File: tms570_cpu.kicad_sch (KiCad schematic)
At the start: 50 parts, among them J3 FTSH-105-01-L-DV-K, U2 TMS570LS0914APGEQQ1

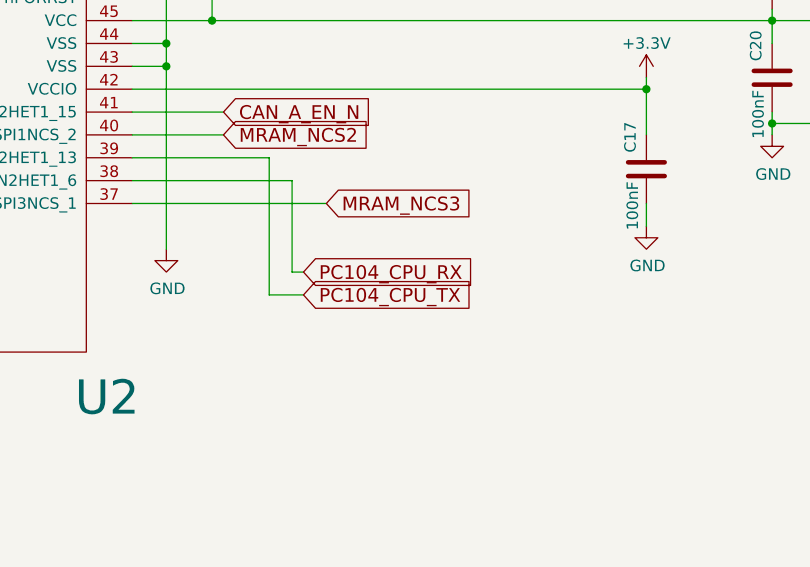
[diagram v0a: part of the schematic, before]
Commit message: Remove the serial connections from the PC104
The USB connection has proven itself, so it shouldn't be needed on later
boards.  This allowed some routing simplification.

Signed-off-by: Corey Minyard <corey@minyard.net>
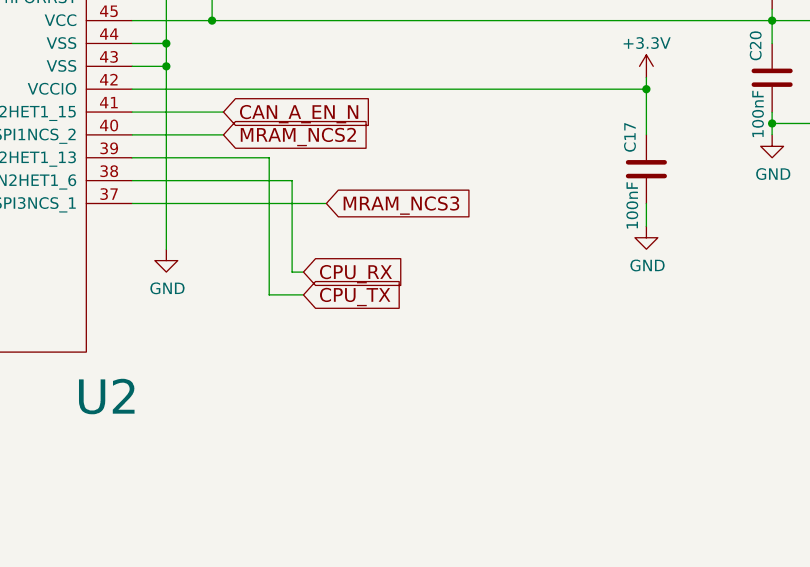
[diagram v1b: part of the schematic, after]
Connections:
- net PC104_CPU_RX renamed CPU_RX
- net PC104_CPU_TX renamed CPU_TX
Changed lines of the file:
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@@
 		)
 	)
-	(global_label "PC104_CPU_TX"
+	(global_label "CPU_TX"
 		(shape input)
 		(at 300.99 193.04 0)
@@
 		)
 	)
-	(global_label "PC104_CPU_RX"
+	(global_label "CPU_RX"
 		(shape input)
 		(at 300.99 190.5 0)

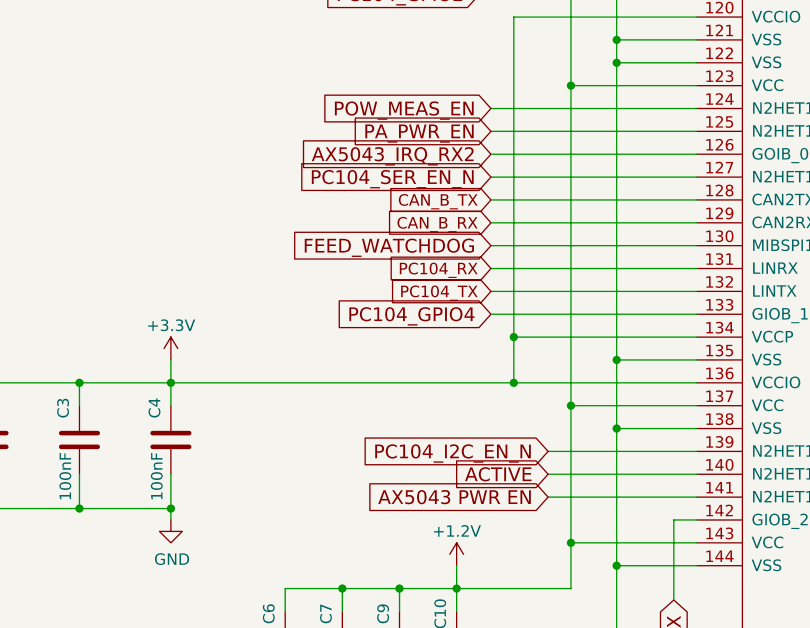
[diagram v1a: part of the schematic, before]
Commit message: Replace the switches for the PC104 I2C and UART with a TMUX2821
It's smaller and has better characteristics.  Particularly, it doesn't
require a pull-up, it's pulled down internally.  Pull down avoids CMOS
latch up on the control pin out of the TMS570.

Signed-off-by: Corey Minyard <corey@minyard.net>
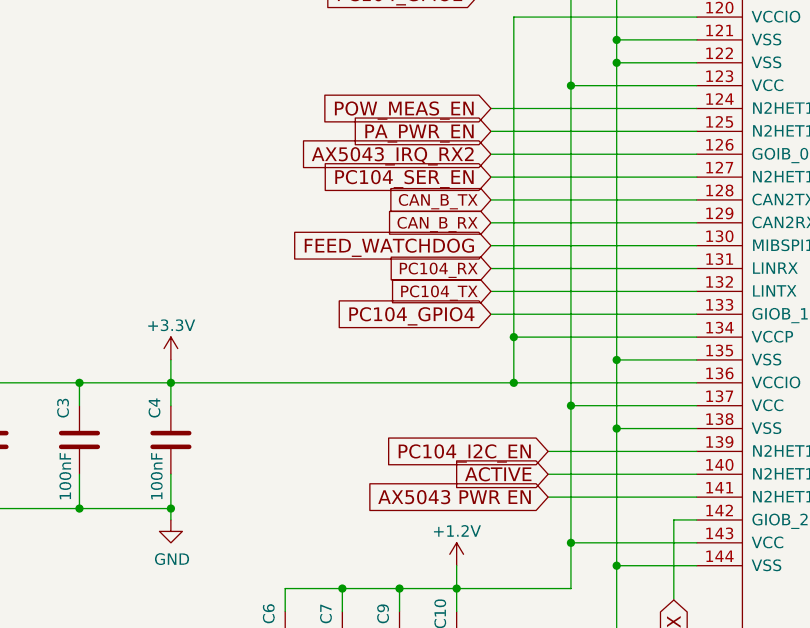
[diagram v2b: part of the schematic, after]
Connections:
- net PC104_I2C_EN_N renamed PC104_I2C_EN
- net PC104_SER_EN_N renamed PC104_SER_EN
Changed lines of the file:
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@@
 		)
 	)
-	(global_label "PC104_SER_EN_N"
+	(global_label "PC104_SER_EN"
 		(shape input)
 		(at 127 142.24 180)
@@
 		)
 	)
-	(global_label "PC104_I2C_EN_N"
+	(global_label "PC104_I2C_EN"
 		(shape input)
 		(at 133.35 172.72 180)

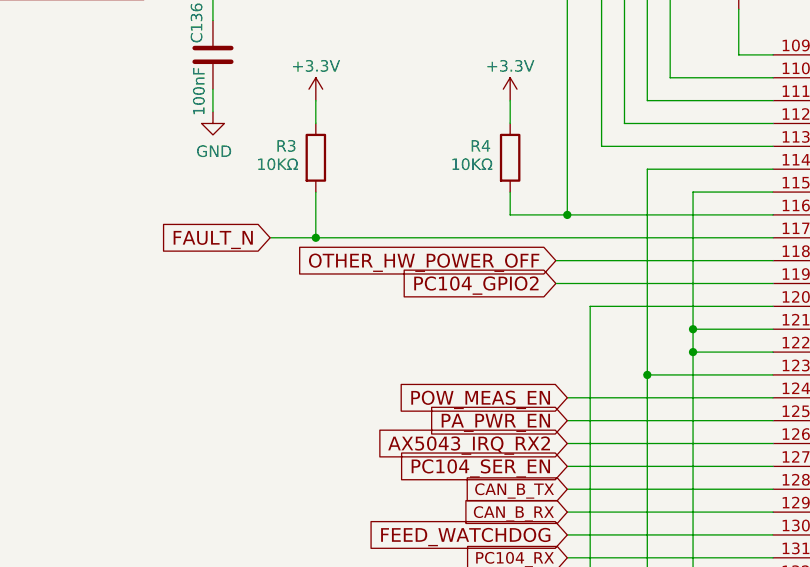
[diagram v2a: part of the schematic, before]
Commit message: Tie the bootstrap load (BSL) lines into the USB chip
Through MOSFETs avoid CMOS latch up.  This will let GPIO lines on the
USB chip start the BSL process.

Signed-off-by: Corey Minyard <corey@minyard.net>
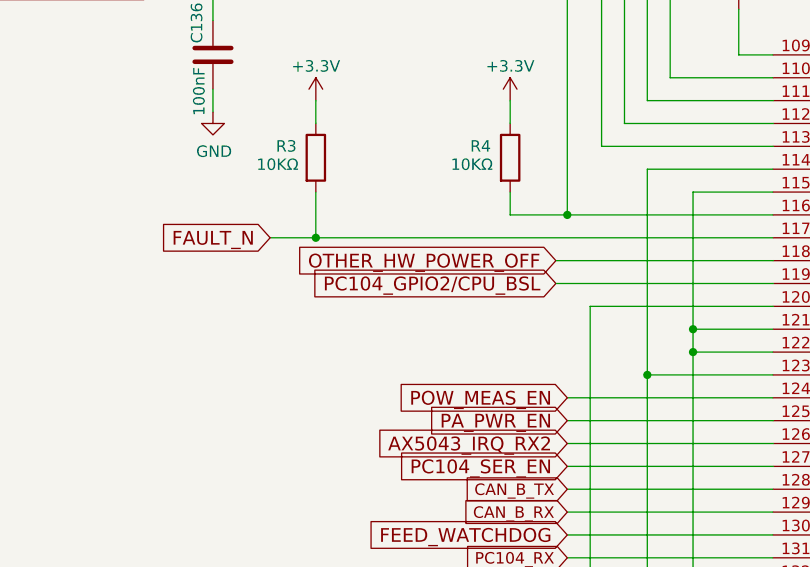
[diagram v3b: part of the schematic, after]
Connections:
- net PC104_GPIO2 renamed PC104_GPIO2/CPU_BSL
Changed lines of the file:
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@@
 		)
 	)
-	(global_label "PC104_GPIO2"
+	(global_label "PC104_GPIO2{slash}CPU_BSL"
 		(shape input)
 		(at 125.73 121.92 180)

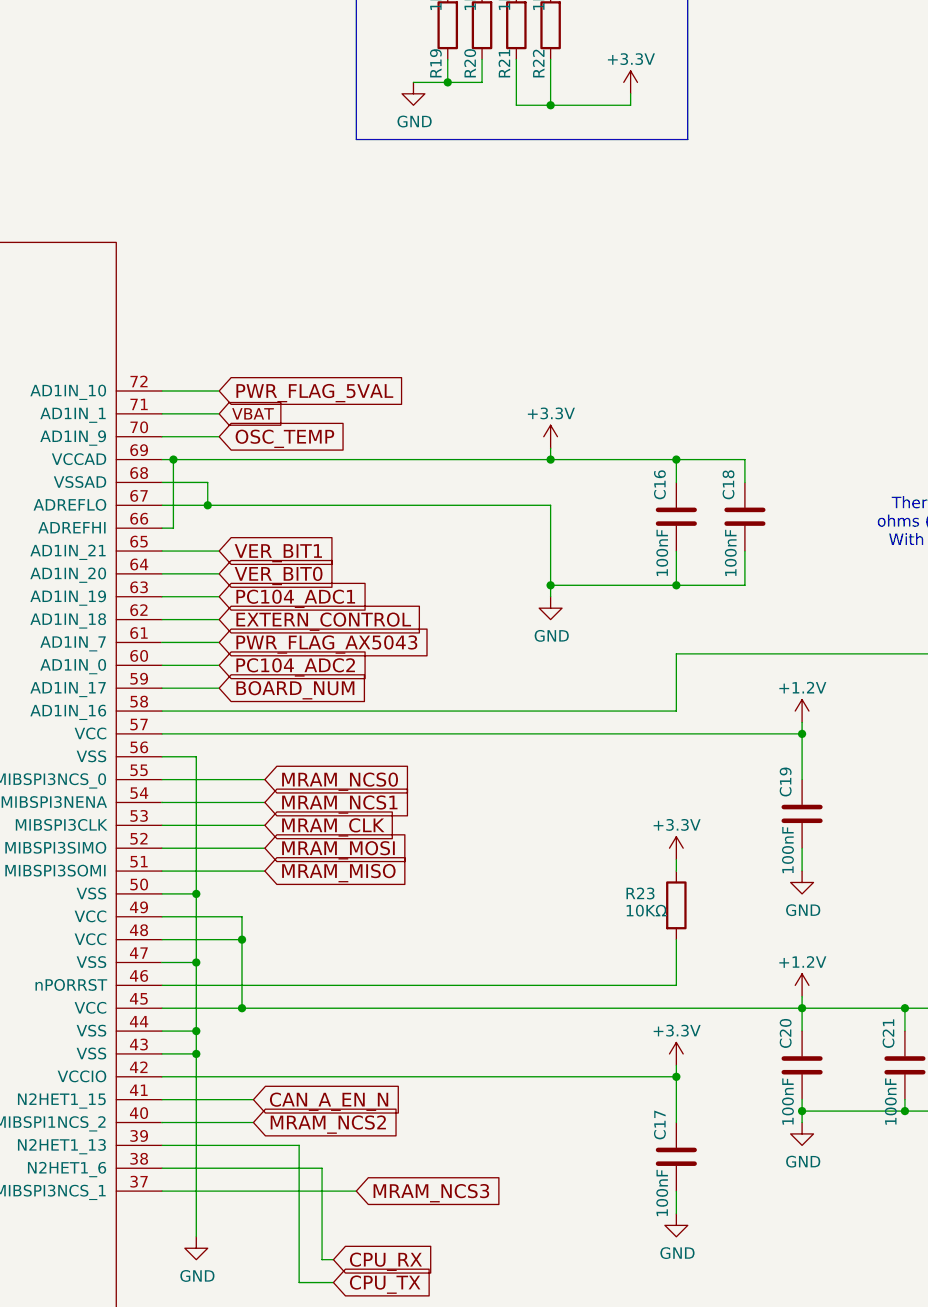
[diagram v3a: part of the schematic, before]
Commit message: Fix various issues from kicad updates
Signed-off-by: Corey Minyard <corey@minyard.net>
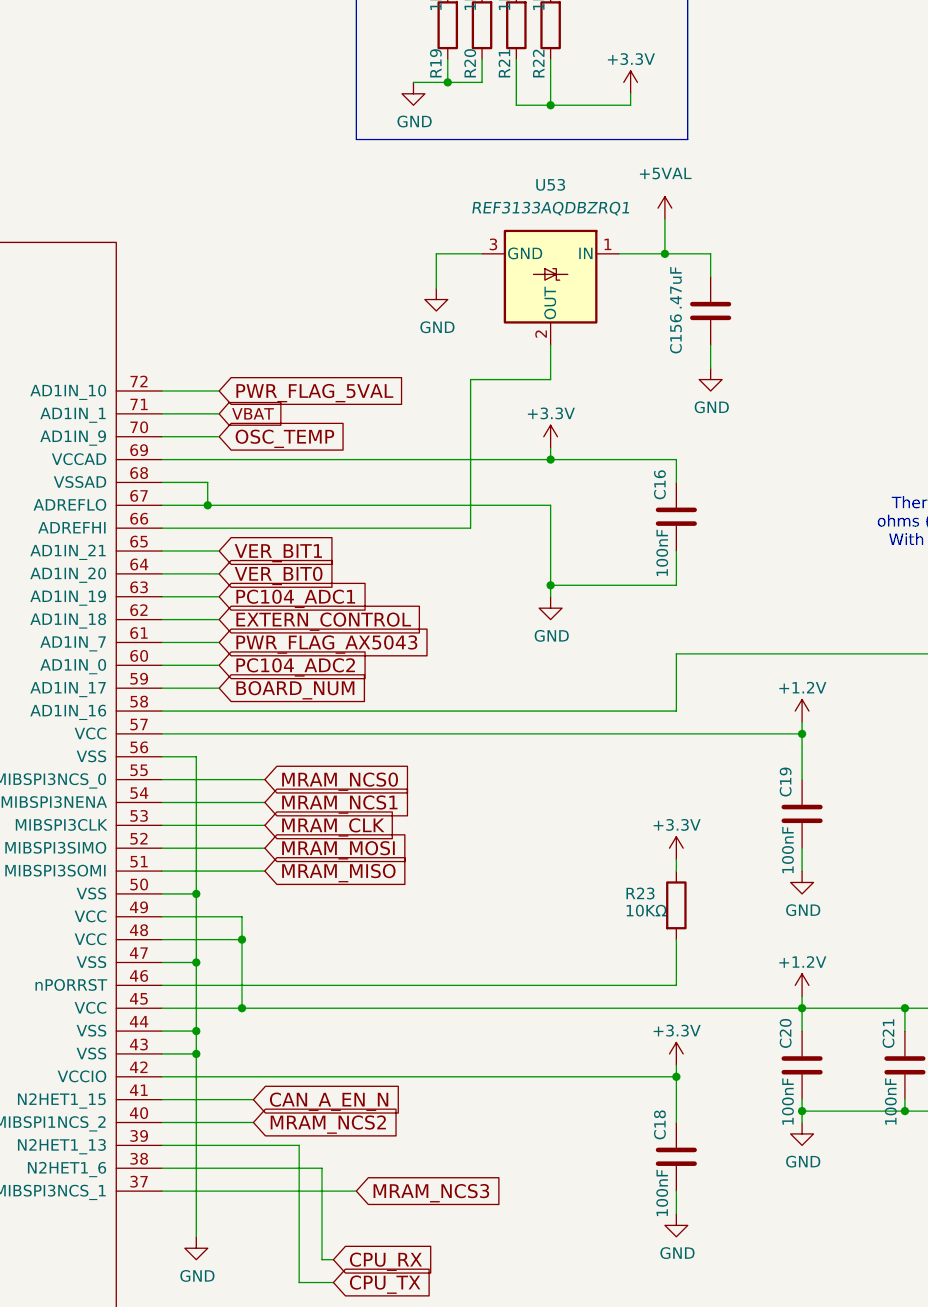
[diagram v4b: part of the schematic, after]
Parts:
- removed C17: 100nF, Capacitor_SMD:C_0402_1005Metric_Pad0.74x0.62mm_HandSolder, symbol Device:C
- added C156: .47uF, Capacitor_SMD:C_0603_1608Metric_Pad1.08x0.95mm_HandSolder, symbol Device:C
- added U53: REF3133AQDBZRQ1, Package_TO_SOT_SMD:SOT-23, symbol PACSAT_ICs:REF3133
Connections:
- net +3.3V: no longer U2.66 (ADREFHI)
- net +5VAL: now also C156.1, U53.1 (IN)
- net GND: now also C156.2, U53.3 (GND)
- new net: U2.66 (ADREFHI), U53.2 (OUT)
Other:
- moved on the sheet: C18

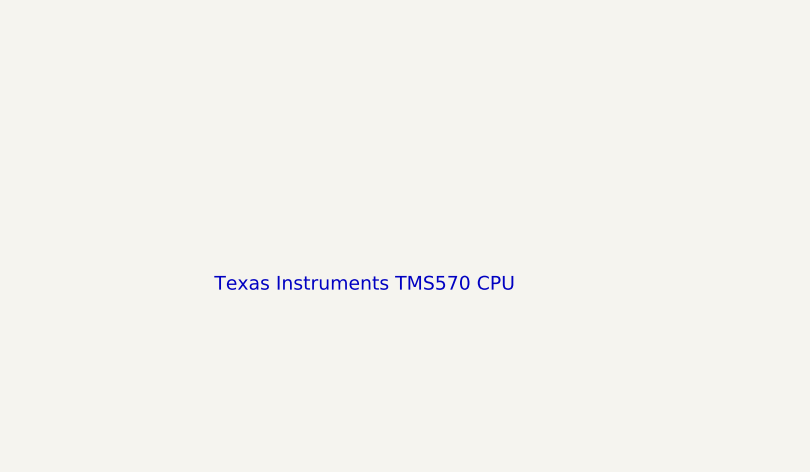
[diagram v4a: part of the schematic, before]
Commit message: Add licensing
Use CERN-OHL-W version 2

Signed-off-by: Corey Minyard <corey@minyard.net>
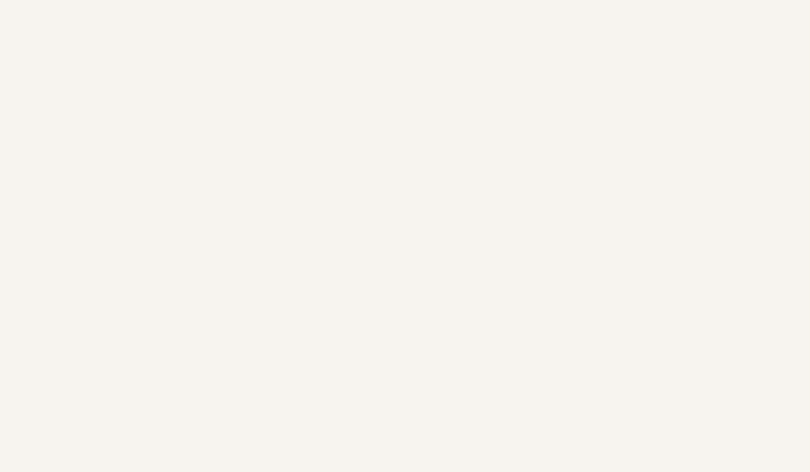
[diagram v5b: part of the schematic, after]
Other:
- note removed: "Texas Instruments TMS570 CPU"
- title: Radiation Tolerant PacSat Communication -> Main Processor
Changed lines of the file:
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@@
 	(paper "USLedger")
 	(title_block
-		(title "Radiation Tolerant PacSat Communication")
-		(date "2023-06-17")
-		(rev "1.1")
+		(title "Main Processor")
+		(date "2026-08-20")
+		(rev "4.0")
 		(company "AMSAT-NA")
-		(comment 1 "N5BRG")
-	)
-	(text "Texas Instruments TMS570 CPU"
-		(exclude_from_sim no)
-		(at 334.01 245.11 0)
-		(effects
-			(font
-				(size 1.524 1.524)
-			)
-			(justify left bottom)
-		)
+		(comment 1 "AE5KM")
+		(comment 2 "Copyright Corey Minyard, 2026")
+		(comment 3 "Licensed under CERN-OHL-W version 2")
 	)
 	(text "RTCK"

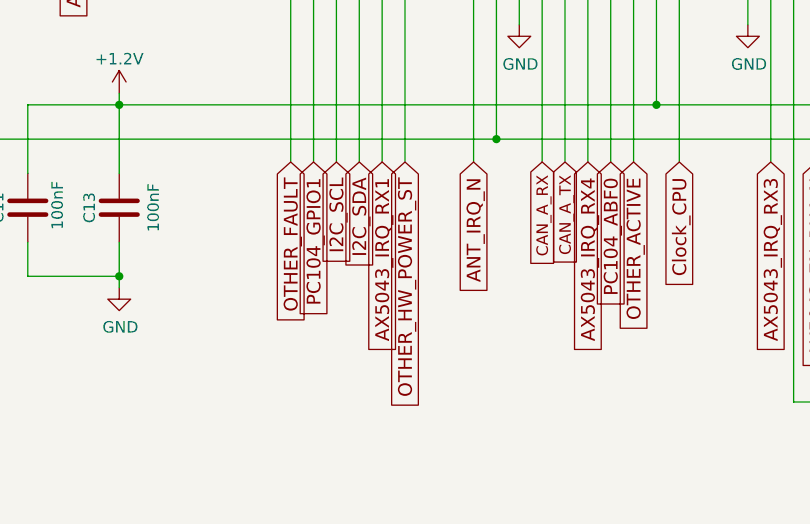
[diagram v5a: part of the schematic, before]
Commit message: Change C125 to .6pF
That has a better notch at 1340MHz.

Signed-off-by: Corey Minyard <corey@minyard.net>
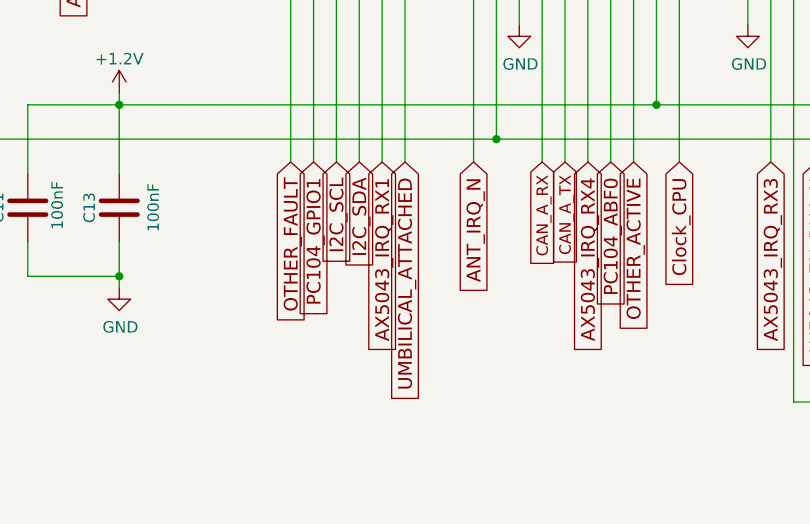
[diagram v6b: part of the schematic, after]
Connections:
- net OTHER_HW_POWER_ST renamed UMBILICAL_ATTACHED
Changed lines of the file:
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@@
 		)
 	)
-	(global_label "OTHER_HW_POWER_ST"
+	(global_label "UMBILICAL_ATTACHED"
 		(shape input)
 		(at 184.15 224.79 270)
@@
 		)
 		(property "Intersheetrefs" "${INTERSHEET_REFS}"
-			(at 184.15 252.0433 90)
+			(at 184.15 251.3176 90)
 			(hide yes)
 			(show_name no)

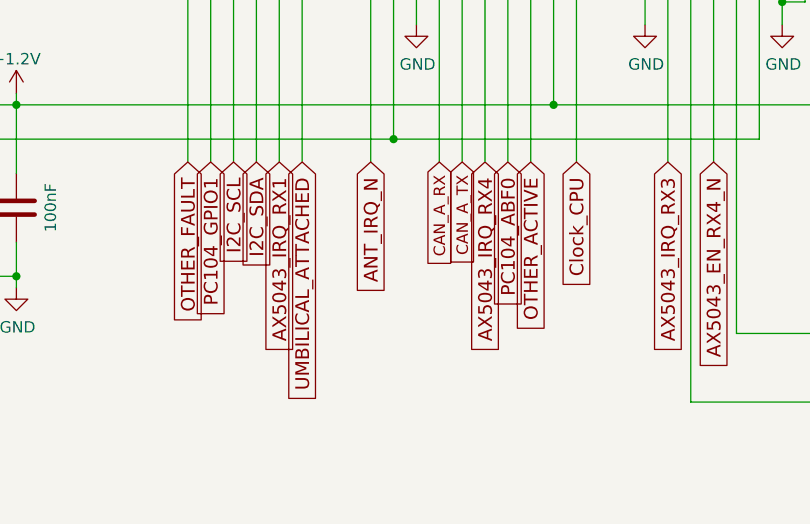
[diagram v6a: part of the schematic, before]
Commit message: Added a tmux2821 for latch-up protection for UMBILICAL_ATTACHED
Ran UMBILICAL_ATTACHED to that, ran UMBILICAL_ATTACHED to the PC104, and
did some renaming on that line.  This will allow other boards to drive
and monitor if an umbilical is attached.  The latchup protection is also
used for the ABF line, and the ABF line is renamed PC104_ABF_N because
it's now negative logic without the MOSFET.

Signed-off-by: Corey Minyard <corey@minyard.net>
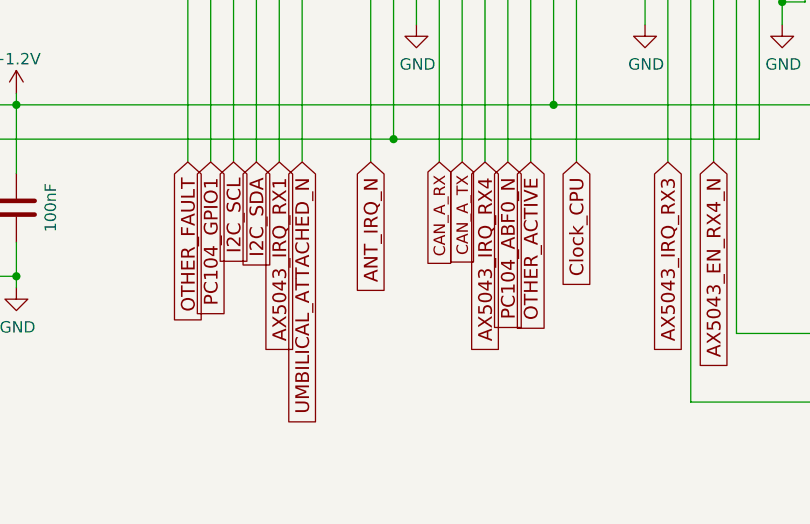
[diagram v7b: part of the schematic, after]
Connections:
- net PC104_ABF0 renamed PC104_ABF0_N
- net UMBILICAL_ATTACHED renamed UMBILICAL_ATTACHED_N
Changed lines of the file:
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@@
 		)
 	)
-	(global_label "UMBILICAL_ATTACHED"
+	(global_label "UMBILICAL_ATTACHED_N"
 		(shape input)
 		(at 184.15 224.79 270)
@@
 		)
 		(property "Intersheetrefs" "${INTERSHEET_REFS}"
-			(at 184.15 251.3176 90)
+			(at 184.15 254.0753 90)
 			(hide yes)
 			(show_name no)
@@
 		)
 	)
-	(global_label "PC104_ABF0"
+	(global_label "PC104_ABF0_N"
 		(shape input)
 		(at 207.01 224.79 270)
@@
 		)
 		(property "Intersheetrefs" "${INTERSHEET_REFS}"
-			(at 207.01 241.7381 90)
-			(hide yes)
-			(show_name no)
+			(at 207.01 244.4958 90)
+			(hide yes)
+			(show_name no)

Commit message: Cost reduce the AX5043 power control
Change the MOSFET + ferrite bead combo on all the AX5043 power inputs
to a inrush-controlled power controller.  The space-rated ferrites are
just too expensive.

Signed-off-by: Corey Minyard <corey@minyard.net>
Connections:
- net AX5043_EN_RX1_N renamed AX5043_EN_RX1
- net AX5043_EN_RX2_N renamed AX5043_EN_RX2
- net AX5043_EN_RX3_N renamed AX5043_EN_RX3
- net AX5043_EN_RX4_N renamed AX5043_EN_RX4
- net AX5043_EN_TX_N renamed AX5043_EN_TX
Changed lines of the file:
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@@
 		)
 	)
-	(global_label "AX5043_EN_RX1_N"
+	(global_label "AX5043_EN_RX1"
 		(shape input)
 		(at 260.35 215.9 270)
@@
 		)
 		(property "Intersheetrefs" "${INTERSHEET_REFS}"
-			(at 260.35 239.7423 90)
+			(at 260.35 236.9846 90)
 			(hide yes)
 			(show_name no)
@@
 		)
 	)
-	(global_label "AX5043_EN_RX4_N"
+	(global_label "AX5043_EN_RX4"
 		(shape input)
 		(at 229.87 224.79 270)
@@
 		)
 		(property "Intersheetrefs" "${INTERSHEET_REFS}"
-			(at 229.87 248.6323 90)
+			(at 229.87 245.8746 90)
 			(hide yes)
 			(show_name no)
@@
 		)
 	)
-	(global_label "AX5043_EN_RX3_N"
+	(global_label "AX5043_EN_RX3"
 		(shape input)
 		(at 252.73 215.9 270)
@@
 		)
 		(property "Intersheetrefs" "${INTERSHEET_REFS}"
-			(at 252.73 239.7423 90)
+			(at 252.73 236.9846 90)
 			(hide yes)
 			(show_name no)
@@
 		)
 	)
-	(global_label "AX5043_EN_TX_N"
+	(global_label "AX5043_EN_TX"
 		(shape input)
 		(at 219.71 59.69 90)
@@
 		)
 		(property "Intersheetrefs" "${INTERSHEET_REFS}"
-			(at 219.71 37.662 90)
+			(at 219.71 40.4197 90)
 			(hide yes)
 			(show_name no)
@@
 		)
 	)
-	(global_label "AX5043_EN_RX2_N"
+	(global_label "AX5043_EN_RX2"
 		(shape input)
 		(at 257.81 215.9 270)
@@
 		)
 		(property "Intersheetrefs" "${INTERSHEET_REFS}"
-			(at 257.81 239.7423 90)
-			(hide yes)
-			(show_name no)
+			(at 257.81 236.9846 90)
+			(hide yes)
+			(show_name no)
